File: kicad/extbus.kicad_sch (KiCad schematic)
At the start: 2 parts, among them J1 Conn_02x40_Counter_Clockwise

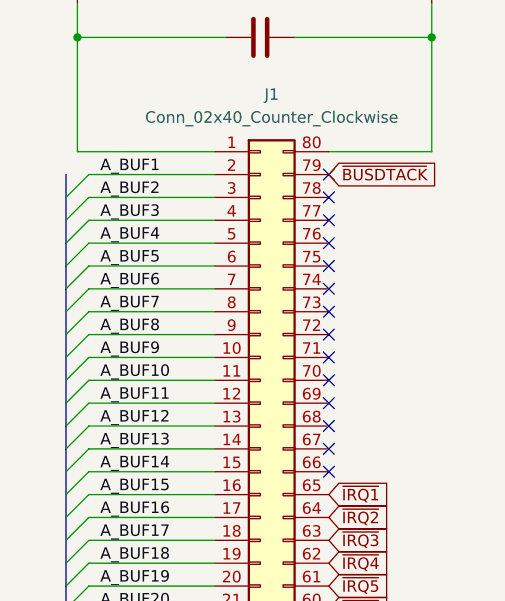
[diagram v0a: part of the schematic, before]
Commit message: Added Bus error handling
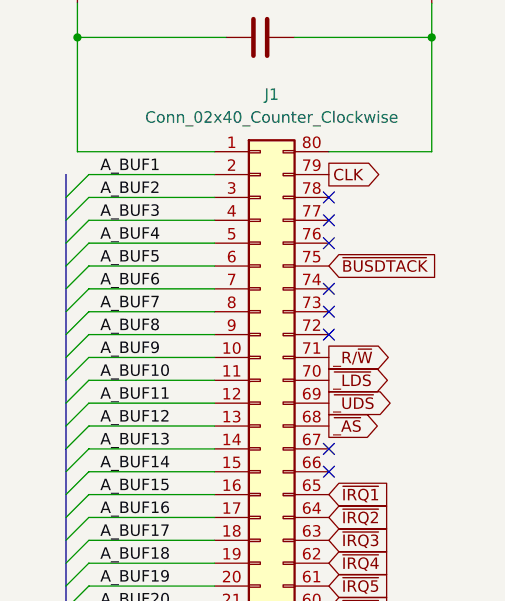
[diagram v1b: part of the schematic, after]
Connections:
- net ~{BUSDTACK}: now also J1.75 (Pin_75); no longer J1.79 (Pin_79)
- net ~{_AS}: now reaches J1.68 (Pin_68)
- net ~{_UDS}: now reaches J1.69 (Pin_69)
- net ~{_LDS}: now reaches J1.70 (Pin_70)
- net _R/~{W}: now reaches J1.71 (Pin_71)
- new net CLK: J1.79 (Pin_79)
- no-connect marks 23 -> 17
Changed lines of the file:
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@@
   (no_connect (at 69.85 127))
   (no_connect (at 82.55 60.96))
-  (no_connect (at 82.55 71.12))
   (no_connect (at 69.85 144.78))
-  (no_connect (at 82.55 68.58))
   (no_connect (at 69.85 134.62))
   (no_connect (at 82.55 144.78))
   (no_connect (at 69.85 129.54))
   (no_connect (at 82.55 53.34))
-  (no_connect (at 82.55 76.2))
   (no_connect (at 82.55 50.8))
-  (no_connect (at 82.55 58.42))
-  (no_connect (at 82.55 48.26))
   (no_connect (at 69.85 142.24))
   (no_connect (at 82.55 78.74))
   (no_connect (at 82.55 55.88))
-  (no_connect (at 82.55 73.66))
   (bus_entry (at 53.34 53.34) (size 2.54 -2.54)
     (stroke (width 0) (type default))
@@
     )
   )
-  (global_label "~{BUSDTACK}" (shape input) (at 82.55 48.26 0) (fields_autoplaced)
-    (effects (font (size 1.27 1.27)) (justify left))
-    (property "Intersheetrefs" "${INTERSHEET_REFS}" (at 95.132 48.26 0)
+  (global_label "~{BUSDTACK}" (shape input) (at 82.55 58.42 0) (fields_autoplaced)
+    (effects (font (size 1.27 1.27)) (justify left))
+    (property "Intersheetrefs" "${INTERSHEET_REFS}" (at 95.132 58.42 0)
+      (effects (font (size 1.27 1.27)) (justify left) hide)
+    )
+  )
+  (global_label "~{_AS}" (shape output) (at 82.55 76.2 0) (fields_autoplaced)
+    (effects (font (size 1.27 1.27)) (justify left))
+    (property "Intersheetrefs" "${INTERSHEET_REFS}" (at 88.7215 76.2 0)
+      (effects (font (size 1.27 1.27)) (justify left) hide)
+    )
+  )
+  (global_label "CLK" (shape output) (at 82.55 48.26 0) (fields_autoplaced)
+    (effects (font (size 1.27 1.27)) (justify left))
+    (property "Intersheetrefs" "${INTERSHEET_REFS}" (at 89.0239 48.26 0)
       (effects (font (size 1.27 1.27)) (justify left) hide)
     )
@@
     )
   )
+  (global_label "_R{slash}~{W}" (shape output) (at 82.55 68.58 0) (fields_autoplaced)
+    (effects (font (size 1.27 1.27)) (justify left))
+    (property "Intersheetrefs" "${INTERSHEET_REFS}" (at 90.4753 68.58 0)
+      (effects (font (size 1.27 1.27)) (justify left) hide)
+    )
+  )
   (global_label "~{IRQ6}" (shape input) (at 82.55 96.52 0) (fields_autoplaced)
     (effects (font (size 1.27 1.27)) (justify left))
@@
       (effects (font (size 1.27 1.27)) (justify left) hide)
     )
+  )
+  (global_label "~{_UDS}" (shape output) (at 82.55 73.66 0) (fields_autoplaced)
+    (effects (font (size 1.27 1.27)) (justify left))
+    (property "Intersheetrefs" "${INTERSHEET_REFS}" (at 90.2334 73.66 0)
+      (effects (font (size 1.27 1.27)) (justify left) hide)
+    )
+  )
+  (global_label "~{_LDS}" (shape output) (at 82.55 71.12 0) (fields_autoplaced)
+    (effects (font (size 1.27 1.27)) (justify left))
+    (property "Intersheetrefs" "${INTERSHEET_REFS}" (at 89.931 71.12 0)
+      (effects (font (size 1.27 1.27)) (justify left) hide)
+    )

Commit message: switched to GALasm
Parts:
- J1: value Conn_02x40_Counter_Clockwise -> BUS Slot #1
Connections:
- net ~{BUSDTACK} renamed ~{DTACK}
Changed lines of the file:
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@@
     (stroke (width 0) (type default))
   )
-  (label "A_BUF3" (at 57.15 53.34 0)
-    (effects (font (size 1.27 1.27)) (justify left bottom))
-  )
-  (label "A_BUF10" (at 57.15 71.12 0)
-    (effects (font (size 1.27 1.27)) (justify left bottom))
-  )
-  (label "D_BUF12" (at 82.55 134.62 0)
-    (effects (font (size 1.27 1.27)) (justify left bottom))
-  )
-  (label "A_BUF18" (at 57.15 91.44 0)
-    (effects (font (size 1.27 1.27)) (justify left bottom))
-  )
-  (label "A_BUF6" (at 57.15 60.96 0)
-    (effects (font (size 1.27 1.27)) (justify left bottom))
-  )
-  (label "D_BUF10" (at 82.55 129.54 0)
-    (effects (font (size 1.27 1.27)) (justify left bottom))
-  )
-  (label "A_BUF9" (at 57.15 68.58 0)
-    (effects (font (size 1.27 1.27)) (justify left bottom))
-  )
-  (label "D_BUF3" (at 82.55 111.76 0)
-    (effects (font (size 1.27 1.27)) (justify left bottom))
-  )
-  (label "A_BUF17" (at 57.15 88.9 0)
-    (effects (font (size 1.27 1.27)) (justify left bottom))
-  )
-  (label "A_BUF11" (at 57.15 73.66 0)
-    (effects (font (size 1.27 1.27)) (justify left bottom))
-  )
-  (label "D_BUF7" (at 82.55 121.92 0)
-    (effects (font (size 1.27 1.27)) (justify left bottom))
-  )
-  (label "D_BUF5" (at 82.55 116.84 0)
-    (effects (font (size 1.27 1.27)) (justify left bottom))
-  )
-  (label "D_BUF8" (at 82.55 124.46 0)
-    (effects (font (size 1.27 1.27)) (justify left bottom))
-  )
-  (label "A_BUF15" (at 57.15 83.82 0)
-    (effects (font (size 1.27 1.27)) (justify left bottom))
-  )
-  (label "A_BUF20" (at 57.15 96.52 0)
-    (effects (font (size 1.27 1.27)) (justify left bottom))
-  )
-  (label "A_BUF12" (at 57.15 76.2 0)
-    (effects (font (size 1.27 1.27)) (justify left bottom))
-  )
-  (label "D_BUF0" (at 82.55 104.14 0)
-    (effects (font (size 1.27 1.27)) (justify left bottom))
-  )
-  (label "D_BUF9" (at 82.55 127 0)
-    (effects (font (size 1.27 1.27)) (justify left bottom))
-  )
-  (label "A_BUF13" (at 57.15 78.74 0)
-    (effects (font (size 1.27 1.27)) (justify left bottom))
-  )
-  (label "A_BUF4" (at 57.15 55.88 0)
-    (effects (font (size 1.27 1.27)) (justify left bottom))
-  )
-  (label "A_BUF16" (at 57.15 86.36 0)
-    (effects (font (size 1.27 1.27)) (justify left bottom))
-  )
-  (label "D_BUF15" (at 82.55 142.24 0)
-    (effects (font (size 1.27 1.27)) (justify left bottom))
-  )
-  (label "A_BUF23" (at 57.15 104.14 0)
-    (effects (font (size 1.27 1.27)) (justify left bottom))
-  )
-  (label "A_BUF1" (at 57.15 48.26 0)
-    (effects (font (size 1.27 1.27)) (justify left bottom))
-  )
-  (label "A_BUF8" (at 57.15 66.04 0)
-    (effects (font (size 1.27 1.27)) (justify left bottom))
-  )
-  (label "A_BUF21" (at 57.15 99.06 0)
-    (effects (font (size 1.27 1.27)) (justify left bottom))
-  )
-  (label "A_BUF14" (at 57.15 81.28 0)
-    (effects (font (size 1.27 1.27)) (justify left bottom))
-  )
-  (label "D_BUF6" (at 82.55 119.38 0)
-    (effects (font (size 1.27 1.27)) (justify left bottom))
-  )
-  (label "A_BUF2" (at 57.15 50.8 0)
-    (effects (font (size 1.27 1.27)) (justify left bottom))
-  )
-  (label "A_BUF5" (at 57.15 58.42 0)
-    (effects (font (size 1.27 1.27)) (justify left bottom))
-  )
-  (label "D_BUF1" (at 82.55 106.68 0)
-    (effects (font (size 1.27 1.27)) (justify left bottom))
-  )
-  (label "D_BUF13" (at 82.55 137.16 0)
-    (effects (font (size 1.27 1.27)) (justify left bottom))
-  )
-  (label "A_BUF22" (at 57.15 101.6 0)
-    (effects (font (size 1.27 1.27)) (justify left bottom))
-  )
-  (label "D_BUF2" (at 82.55 109.22 0)
-    (effects (font (size 1.27 1.27)) (justify left bottom))
-  )
-  (label "A_BUF19" (at 57.15 93.98 0)
-    (effects (font (size 1.27 1.27)) (justify left bottom))
-  )
-  (label "A_BUF7" (at 57.15 63.5 0)
-    (effects (font (size 1.27 1.27)) (justify left bottom))
-  )
-  (label "D_BUF11" (at 82.55 132.08 0)
-    (effects (font (size 1.27 1.27)) (justify left bottom))
-  )
-  (label "D_BUF4" (at 82.55 114.3 0)
-    (effects (font (size 1.27 1.27)) (justify left bottom))
-  )
-  (label "D_BUF14" (at 82.55 139.7 0)
+  (label "A_BUF3" (at 57.15 53.34 0) (fields_autoplaced)
+    (effects (font (size 1.27 1.27)) (justify left bottom))
+  )
+  (label "A_BUF10" (at 57.15 71.12 0) (fields_autoplaced)
+    (effects (font (size 1.27 1.27)) (justify left bottom))
+  )
+  (label "D_BUF12" (at 82.55 134.62 0) (fields_autoplaced)
+    (effects (font (size 1.27 1.27)) (justify left bottom))
+  )
+  (label "A_BUF18" (at 57.15 91.44 0) (fields_autoplaced)
+    (effects (font (size 1.27 1.27)) (justify left bottom))
+  )
+  (label "A_BUF6" (at 57.15 60.96 0) (fields_autoplaced)
+    (effects (font (size 1.27 1.27)) (justify left bottom))
+  )
+  (label "D_BUF10" (at 82.55 129.54 0) (fields_autoplaced)
+    (effects (font (size 1.27 1.27)) (justify left bottom))
+  )
+  (label "A_BUF9" (at 57.15 68.58 0) (fields_autoplaced)
+    (effects (font (size 1.27 1.27)) (justify left bottom))
+  )
+  (label "D_BUF3" (at 82.55 111.76 0) (fields_autoplaced)
+    (effects (font (size 1.27 1.27)) (justify left bottom))
+  )
+  (label "A_BUF17" (at 57.15 88.9 0) (fields_autoplaced)
+    (effects (font (size 1.27 1.27)) (justify left bottom))
+  )
+  (label "A_BUF11" (at 57.15 73.66 0) (fields_autoplaced)
+    (effects (font (size 1.27 1.27)) (justify left bottom))
+  )
+  (label "D_BUF7" (at 82.55 121.92 0) (fields_autoplaced)
+    (effects (font (size 1.27 1.27)) (justify left bottom))
+  )
+  (label "D_BUF5" (at 82.55 116.84 0) (fields_autoplaced)
+    (effects (font (size 1.27 1.27)) (justify left bottom))
+  )
+  (label "D_BUF8" (at 82.55 124.46 0) (fields_autoplaced)
+    (effects (font (size 1.27 1.27)) (justify left bottom))
+  )
+  (label "A_BUF15" (at 57.15 83.82 0) (fields_autoplaced)
+    (effects (font (size 1.27 1.27)) (justify left bottom))
+  )
+  (label "A_BUF20" (at 57.15 96.52 0) (fields_autoplaced)
+    (effects (font (size 1.27 1.27)) (justify left bottom))
+  )
+  (label "A_BUF12" (at 57.15 76.2 0) (fields_autoplaced)
+    (effects (font (size 1.27 1.27)) (justify left bottom))
+  )
+  (label "D_BUF0" (at 82.55 104.14 0) (fields_autoplaced)
+    (effects (font (size 1.27 1.27)) (justify left bottom))
+  )
+  (label "D_BUF9" (at 82.55 127 0) (fields_autoplaced)
+    (effects (font (size 1.27 1.27)) (justify left bottom))
+  )
+  (label "A_BUF13" (at 57.15 78.74 0) (fields_autoplaced)
+    (effects (font (size 1.27 1.27)) (justify left bottom))
+  )
+  (label "A_BUF4" (at 57.15 55.88 0) (fields_autoplaced)
+    (effects (font (size 1.27 1.27)) (justify left bottom))
+  )
+  (label "A_BUF16" (at 57.15 86.36 0) (fields_autoplaced)
+    (effects (font (size 1.27 1.27)) (justify left bottom))
+  )
+  (label "D_BUF15" (at 82.55 142.24 0) (fields_autoplaced)
+    (effects (font (size 1.27 1.27)) (justify left bottom))
+  )
+  (label "A_BUF23" (at 57.15 104.14 0) (fields_autoplaced)
+    (effects (font (size 1.27 1.27)) (justify left bottom))
+  )
+  (label "A_BUF1" (at 57.15 48.26 0) (fields_autoplaced)
+    (effects (font (size 1.27 1.27)) (justify left bottom))
+  )
+  (label "A_BUF8" (at 57.15 66.04 0) (fields_autoplaced)
+    (effects (font (size 1.27 1.27)) (justify left bottom))
+  )
+  (label "A_BUF21" (at 57.15 99.06 0) (fields_autoplaced)
+    (effects (font (size 1.27 1.27)) (justify left bottom))
+  )
+  (label "A_BUF14" (at 57.15 81.28 0) (fields_autoplaced)
+    (effects (font (size 1.27 1.27)) (justify left bottom))
+  )
+  (label "D_BUF6" (at 82.55 119.38 0) (fields_autoplaced)
+    (effects (font (size 1.27 1.27)) (justify left bottom))
+  )
+  (label "A_BUF2" (at 57.15 50.8 0) (fields_autoplaced)
+    (effects (font (size 1.27 1.27)) (justify left bottom))
+  )
+  (label "A_BUF5" (at 57.15 58.42 0) (fields_autoplaced)
+    (effects (font (size 1.27 1.27)) (justify left bottom))
+  )
+  (label "D_BUF1" (at 82.55 106.68 0) (fields_autoplaced)
+    (effects (font (size 1.27 1.27)) (justify left bottom))
+  )
+  (label "D_BUF13" (at 82.55 137.16 0) (fields_autoplaced)
+    (effects (font (size 1.27 1.27)) (justify left bottom))
+  )
+  (label "A_BUF22" (at 57.15 101.6 0) (fields_autoplaced)
+    (effects (font (size 1.27 1.27)) (justify left bottom))
+  )
+  (label "D_BUF2" (at 82.55 109.22 0) (fields_autoplaced)
+    (effects (font (size 1.27 1.27)) (justify left bottom))
+  )
+  (label "A_BUF19" (at 57.15 93.98 0) (fields_autoplaced)
+    (effects (font (size 1.27 1.27)) (justify left bottom))
+  )
+  (label "A_BUF7" (at 57.15 63.5 0) (fields_autoplaced)
+    (effects (font (size 1.27 1.27)) (justify left bottom))
+  )
+  (label "D_BUF11" (at 82.55 132.08 0) (fields_autoplaced)
+    (effects (font (size 1.27 1.27)) (justify left bottom))
+  )
+  (label "D_BUF4" (at 82.55 114.3 0) (fields_autoplaced)
+    (effects (font (size 1.27 1.27)) (justify left bottom))
+  )
+  (label "D_BUF14" (at 82.55 139.7 0) (fields_autoplaced)
     (effects (font (size 1.27 1.27)) (justify left bottom))
   )
@@
     )
   )
-  (global_label "~{BUSDTACK}" (shape input) (at 82.55 58.42 0) (fields_autoplaced)
-    (effects (font (size 1.27 1.27)) (justify left))
-    (property "Intersheetrefs" "${INTERSHEET_REFS}" (at 95.132 58.42 0)
+  (global_label "~{DTACK}" (shape input) (at 82.55 58.42 0) (fields_autoplaced)
+    (effects (font (size 1.27 1.27)) (justify left))
+    (property "Intersheetrefs" "${INTERSHEET_REFS}" (at 91.322 58.42 0)
       (effects (font (size 1.27 1.27)) (justify left) hide)
     )
@@
       (effects (font (size 1.27 1.27)))
     )
-    (property "Value" "Conn_02x40_Counter_Clockwise" (at 76.2 41.91 0)
+    (property "Value" "BUS Slot #1" (at 76.2 41.91 0)
       (effects (font (size 1.27 1.27)))
     )
